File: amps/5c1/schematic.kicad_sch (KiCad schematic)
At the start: 21 parts, among them T1 SE 5k:8

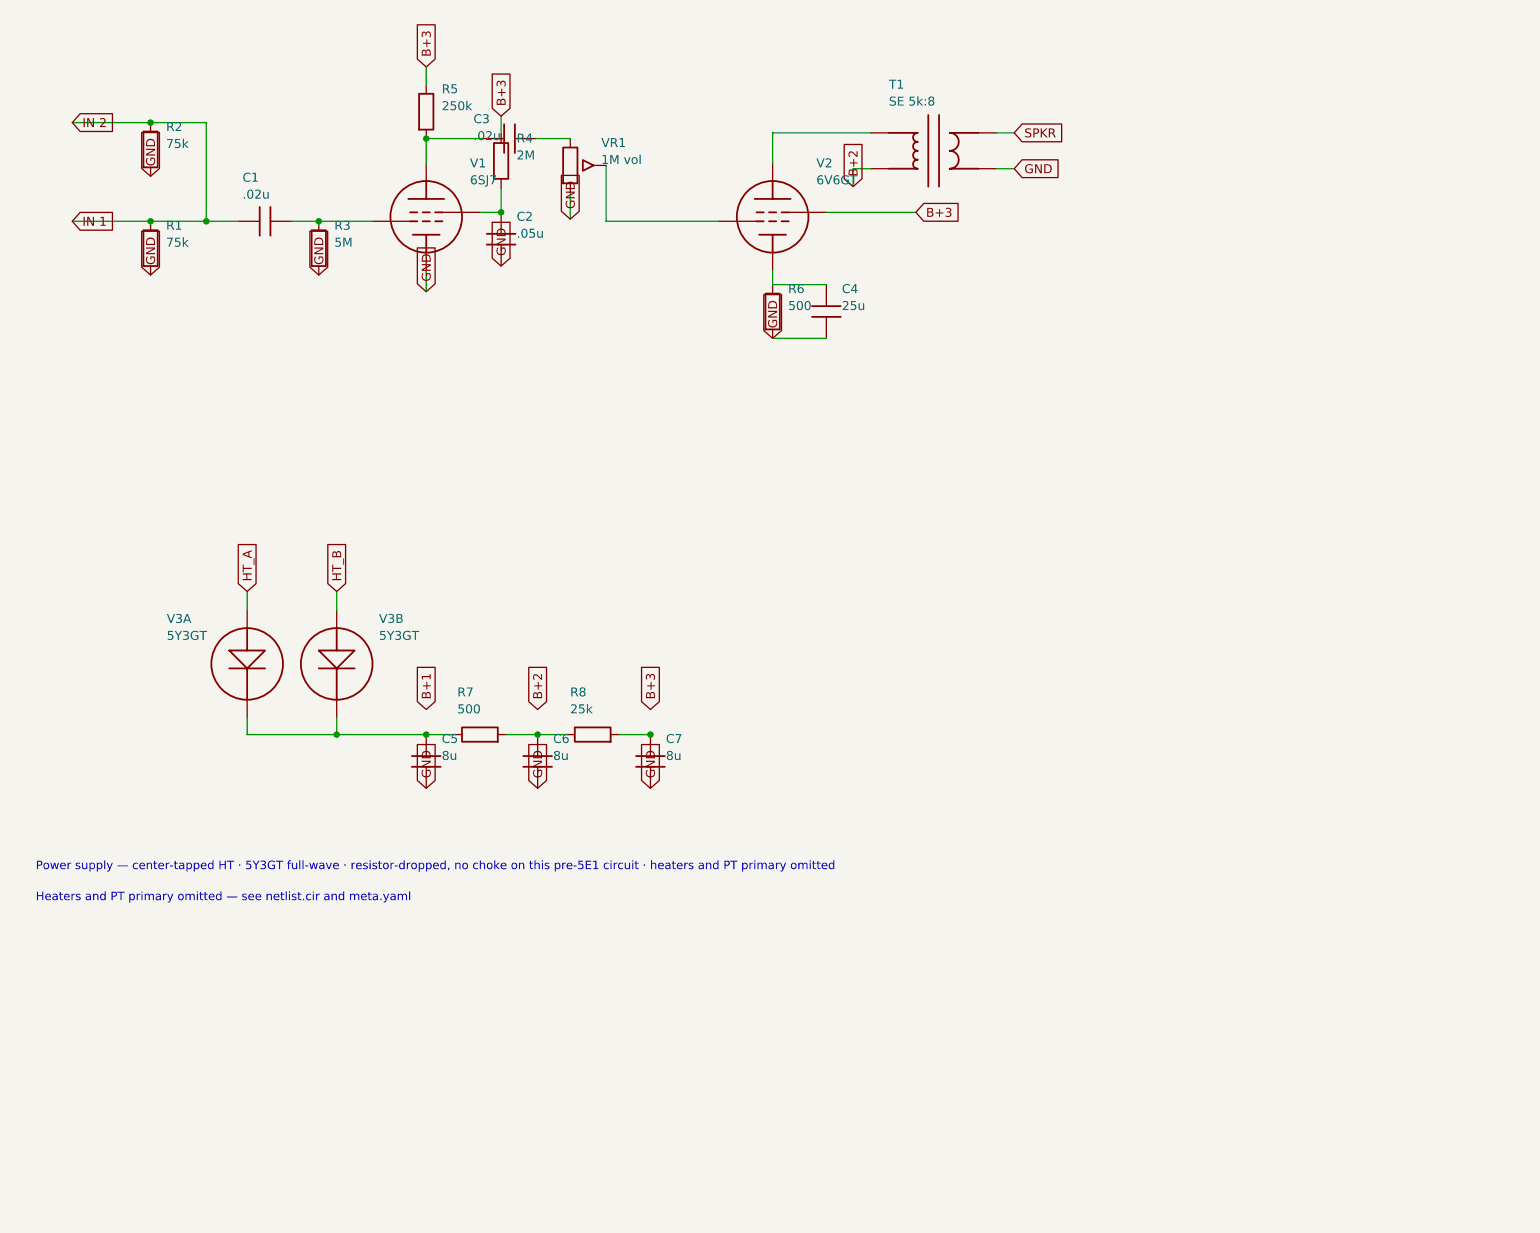
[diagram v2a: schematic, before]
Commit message: Fix: rotated global labels lettered their net names outside the flag
Every global label this pipeline emitted carried (justify left) regardless of
rotation. KiCanvas — like KiCad — draws label text horizontally at 0/180 and
vertically at 90/270 and reads WHICH SIDE of the anchor it letters on from the
justification, so at 180 and 270 the name printed outside an empty flag
outline, struck through by the very wire it names: 219 labels at 180 deg
(including the input-jack flags at top-left of nearly every sheet, the first
glyphs a visitor reads) and 792 GND/rail flags at 270 whose names squeezed at
the flag mouth instead of lettering down the body. The library already
compensated rotation for property text (`pa`); this mirrors that logic for
global labels: justify right at 180/270, left at 0/90.

check_schematics gains the geometry clause whose absence let all 1011
instances through a "no lettering through circuitry" pass: it modelled the
flag box but never the label TEXT, so a name rendered on the wrong side was
invisible to it. The gate now proves justification compensates rotation on
every global label.

Two more things this exposed, fixed in the same engine pass:

- Placement now measures with the renderer's own Newstroke advance table
  (extracted from the vendored kicanvas.js) instead of a flat 0.68-em prose
  average that under-read part lettering by a quarter — the mechanism behind
  every "metered clean, printed through its neighbour" incident. The GATE
  deliberately keeps the coarse ruler: re-ruling it with renderer truth was
  tried and red-flagged 28 of 34 sheets over abutments three visual passes
  had already judged sub-visual (the two-rulers note in schematic_lib.py).
- place_captions' escape ladder runs further, because a banner caption
  measured truly is half again wider than the old estimate believed.

All 34 schematics regenerated; full gate suite green.

🤖 Generated with [Claude Code](https://claude.com/claude-code)

Co-Authored-By: Claude Fable 5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
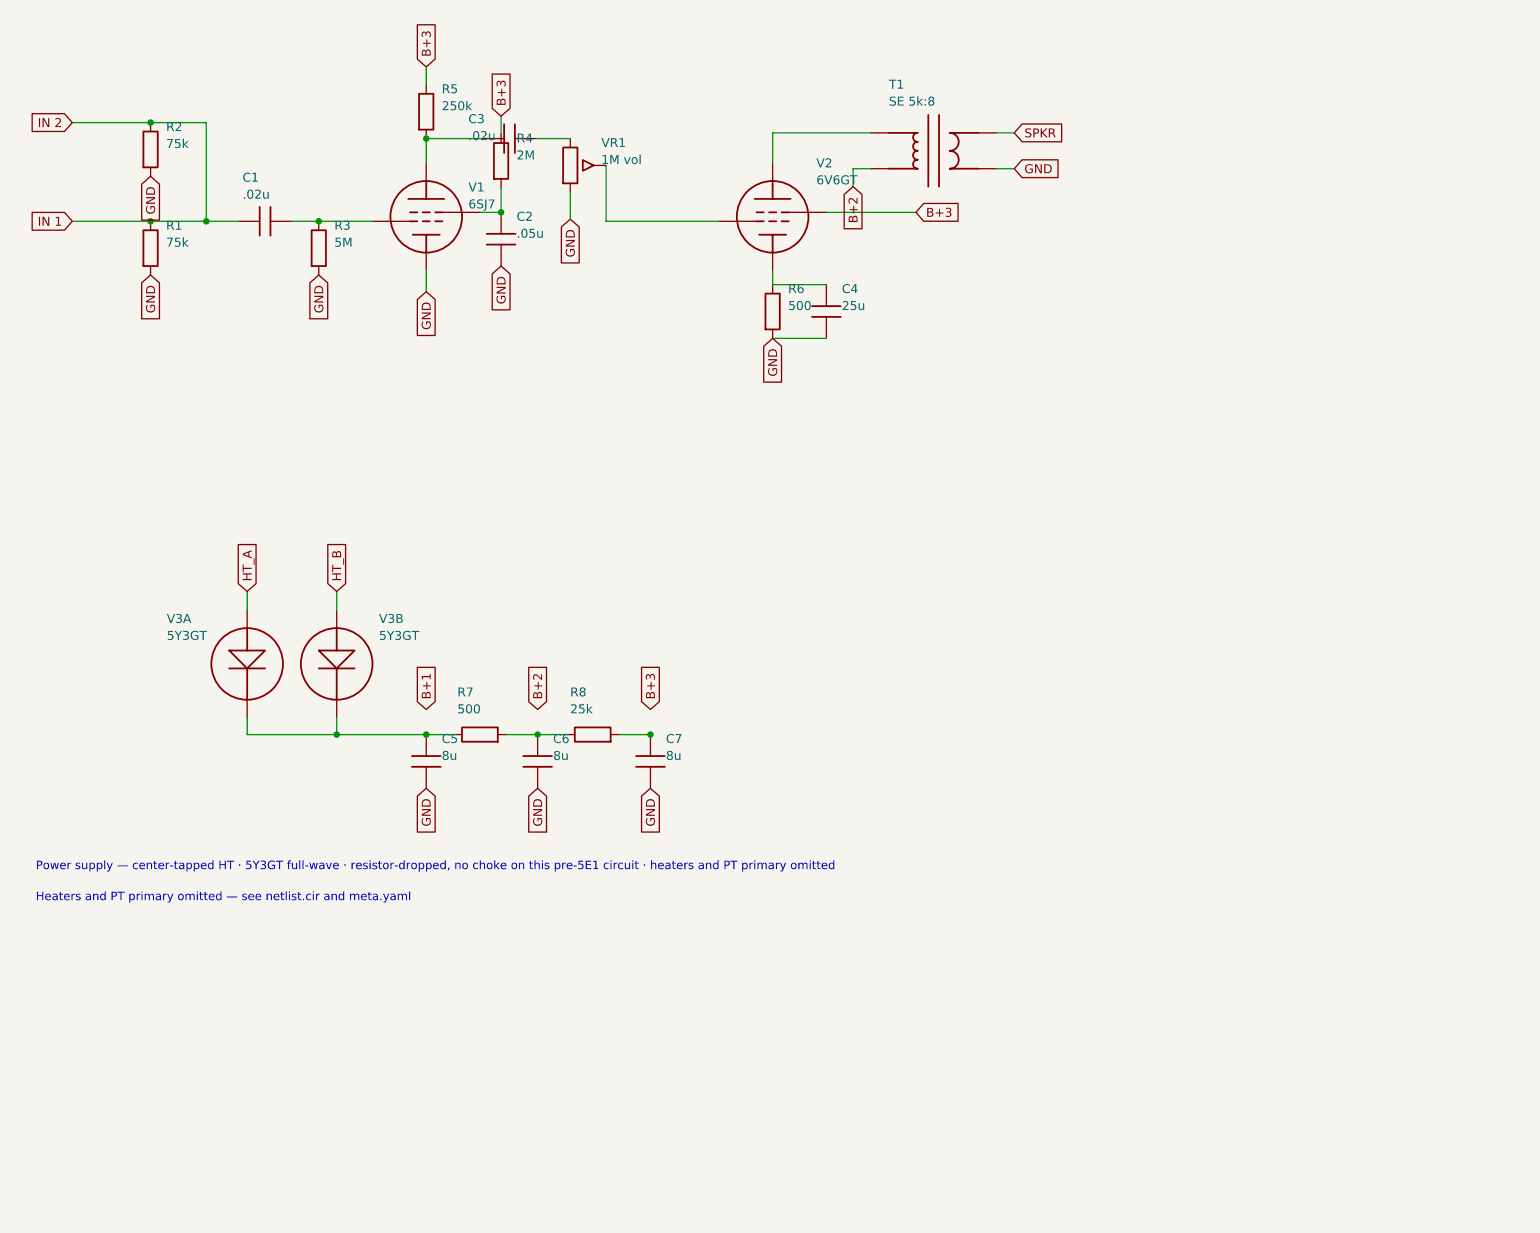
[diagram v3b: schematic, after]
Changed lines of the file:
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@@
     (comment 3 "Values read from: https://el34world.com/charts/Schematics/files/Fender/Fender_champ_5c1_schem.pdf"))
   (global_label "IN 1" (shape input) (at 17.8816 38.913 180)
-    (effects (font (size 1.27 1.27)) (justify left)))
+    (effects (font (size 1.27 1.27)) (justify right)))
   (wire (pts (xy 17.8816 38.913) (xy 28.9816 38.913))
     (stroke (width 0) (type default)))
@@
     (property "Value" "75k" (at 31.1816 41.923 0) (effects (font (size 1.27 1.27)) (justify left))))
   (global_label "GND" (shape input) (at 28.9816 46.533 270)
-    (effects (font (size 1.27 1.27)) (justify left)))
+    (effects (font (size 1.27 1.27)) (justify right)))
   (wire (pts (xy 28.9816 38.913) (xy 36.8816 38.913))
     (stroke (width 0) (type default)))
   (global_label "IN 2" (shape input) (at 17.8816 24.913 180)
-    (effects (font (size 1.27 1.27)) (justify left)))
+    (effects (font (size 1.27 1.27)) (justify right)))
   (wire (pts (xy 17.8816 24.913) (xy 28.9816 24.913))
     (stroke (width 0) (type default)))
@@
     (property "Value" "75k" (at 31.1816 27.923 0) (effects (font (size 1.27 1.27)) (justify left))))
   (global_label "GND" (shape input) (at 28.9816 32.533 270)
-    (effects (font (size 1.27 1.27)) (justify left)))
+    (effects (font (size 1.27 1.27)) (justify right)))
   (wire (pts (xy 28.9816 24.913) (xy 36.8816 24.913))
     (stroke (width 0) (type default)))
@@
     (property "Value" "5M" (at 55.0416 41.923 0) (effects (font (size 1.27 1.27)) (justify left))))
   (global_label "GND" (shape input) (at 52.8416 46.533 270)
-    (effects (font (size 1.27 1.27)) (justify left)))
+    (effects (font (size 1.27 1.27)) (justify right)))
   (wire (pts (xy 52.8416 38.913) (xy 60.4616 38.913))
     (stroke (width 0) (type default)))
   (symbol (lib_id "cx:PENTODE") (at 68.0816 38.278 0) (unit 1)
     (in_bom yes) (on_board yes)
-    (property "Reference" "V1" (at 74.2816 30.678 0) (effects (font (size 1.27 1.27)) (justify left)))
-    (property "Value" "6SJ7" (at 74.2816 33.078 0) (effects (font (size 1.27 1.27)) (justify left))))
+    (property "Reference" "V1" (at 74.0616 34.098 0) (effects (font (size 1.27 1.27)) (justify left)))
+    (property "Value" "6SJ7" (at 74.0616 36.498 0) (effects (font (size 1.27 1.27)) (justify left))))
   (wire (pts (xy 68.0816 45.898) (xy 68.0816 48.898))
     (stroke (width 0) (type default)))
   (global_label "GND" (shape input) (at 68.0816 48.898 270)
-    (effects (font (size 1.27 1.27)) (justify left)))
+    (effects (font (size 1.27 1.27)) (justify right)))
   (wire (pts (xy 68.0816 30.658) (xy 68.0816 27.178))
     (stroke (width 0) (type default)))
@@
   (symbol (lib_id "cx:C") (at 79.8916 27.178 90) (unit 1)
     (in_bom yes) (on_board yes)
-    (property "Reference" "C3" (at 74.7752 24.41 270) (effects (font (size 1.27 1.27)) (justify left)))
-    (property "Value" ".02u" (at 74.7752 26.81 270) (effects (font (size 1.27 1.27)) (justify left))))
+    (property "Reference" "C3" (at 74.0576 24.41 270) (effects (font (size 1.27 1.27)) (justify left)))
+    (property "Value" ".02u" (at 74.0576 26.81 270) (effects (font (size 1.27 1.27)) (justify left))))
   (wire (pts (xy 75.7016 37.643) (xy 78.7016 37.643))
     (stroke (width 0) (type default)))
@@
     (property "Value" ".05u" (at 80.9016 40.653 0) (effects (font (size 1.27 1.27)) (justify left))))
   (global_label "GND" (shape input) (at 78.7016 45.263 270)
-    (effects (font (size 1.27 1.27)) (justify left)))
+    (effects (font (size 1.27 1.27)) (justify right)))
   (wire (pts (xy 78.7016 37.643) (xy 78.7016 34.163))
     (stroke (width 0) (type default)))
@@
     (stroke (width 0) (type default)))
   (global_label "GND" (shape input) (at 88.5116 38.608 270)
-    (effects (font (size 1.27 1.27)) (justify left)))
+    (effects (font (size 1.27 1.27)) (justify right)))
   (wire (pts (xy 93.5916 30.988) (xy 93.5916 38.913))
     (stroke (width 0) (type default)))
@@
     (stroke (width 0) (type default)))
   (global_label "GND" (shape input) (at 117.212 55.518 270)
-    (effects (font (size 1.27 1.27)) (justify left)))
+    (effects (font (size 1.27 1.27)) (justify right)))
   (symbol (lib_id "cx:OT_SE") (at 140.052 28.913 0) (unit 1)
     (in_bom yes) (on_board yes)
@@
     (stroke (width 0) (type default)))
   (global_label "B+2" (shape input) (at 128.622 33.993 270)
-    (effects (font (size 1.27 1.27)) (justify left)))
+    (effects (font (size 1.27 1.27)) (justify right)))
   (wire (pts (xy 148.942 26.373) (xy 151.482 26.373))
     (stroke (width 0) (type default)))
@@
     (property "Value" "8u" (at 70.2816 114.723 0) (effects (font (size 1.27 1.27)) (justify left))))
   (global_label "GND" (shape input) (at 68.0816 119.333 270)
-    (effects (font (size 1.27 1.27)) (justify left)))
+    (effects (font (size 1.27 1.27)) (justify right)))
   (global_label "B+1" (shape input) (at 68.0816 108.153 90)
     (effects (font (size 1.27 1.27)) (justify left)))
@@
     (property "Value" "8u" (at 86.0816 114.723 0) (effects (font (size 1.27 1.27)) (justify left))))
   (global_label "GND" (shape input) (at 83.8816 119.333 270)
-    (effects (font (size 1.27 1.27)) (justify left)))
+    (effects (font (size 1.27 1.27)) (justify right)))
   (global_label "B+2" (shape input) (at 83.8816 108.153 90)
     (effects (font (size 1.27 1.27)) (justify left)))
@@
     (property "Value" "8u" (at 102.082 114.723 0) (effects (font (size 1.27 1.27)) (justify left))))
   (global_label "GND" (shape input) (at 99.8816 119.333 270)
-    (effects (font (size 1.27 1.27)) (justify left)))
+    (effects (font (size 1.27 1.27)) (justify right)))
   (global_label "B+3" (shape input) (at 99.8816 108.153 90)
     (effects (font (size 1.27 1.27)) (justify left)))

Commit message: Fix: deterministic schematic ids and wires split at every join
- _u() is uuid5 over (amp id, emission order), so a regeneration of an
  unchanged script is byte-identical and a drift gate becomes possible
- write() splits wire segments at symbol pins, wire ends and junction dots,
  so the file connects exactly what the drawing shows under KiCad's
  endpoint-only semantics (270 pins were on a wire's interior; net
  partitions unchanged on all 38 sheets)
- all sheets regenerated; aa864-bassman title block was stale (draft) and
  now matches meta.yaml (verified)

Co-Authored-By: Claude Fable 5.1 <noreply@anthropic.com>
Claude-Session: https://claude.ai/code/session_01KBMfdh37HmCL2iWcBiL5J1
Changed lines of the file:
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@@
   (wire (pts (xy 55.3816 109.313) (xy 55.3816 111.713))
     (stroke (width 0) (type default)))
-  (wire (pts (xy 42.6816 111.713) (xy 68.0816 111.713))
+  (wire (pts (xy 42.6816 111.713) (xy 55.3816 111.713))
+    (stroke (width 0) (type default)))
+  (wire (pts (xy 55.3816 111.713) (xy 68.0816 111.713))
     (stroke (width 0) (type default)))
   (junction (at 55.3816 111.713) (diameter 0) (color 0 0 0 0))

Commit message: Fix: schematic wiring on 5c1, 5e1, 5e4a, 5e5a, 5e6a, 5f4; all six claim equivalence
- 5c1, 5e1: the B+1/B+2/B+3 labels sat 3.56 mm above the filter chain with
  no lead, naming rails the drawing never reached
- 5e4a, 5e5a, 5e6a, 5f4: the 220k grid leak tapped the coupling-cap node;
  the netlist and the factory-derived layouts both return it at the grid
  pin after the 1.5k stopper (coupler -> stopper -> grid, as jtm45 draws
  it); each stopper now lands on the pentode's own grid pin and the leak
  hangs off that junction
- sch_map.yaml schematic_claim: verified on all six -> 37 of 38 sheets are
  hard-gated; 6g5 stays unclaimed (presence-branch DC path is a source
  question, not a declaration)

Co-Authored-By: Claude Fable 5.1 <noreply@anthropic.com>
Claude-Session: https://claude.ai/code/session_01KBMfdh37HmCL2iWcBiL5J1
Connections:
- net B+1: now also C5.1, R7.1, V3A.2 (K), V3B.2 (K)
- net B+2: now also C6.1, R7.2, R8.1
- net B+3: now also C7.1, R8.2
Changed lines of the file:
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@@
   (global_label "GND" (shape input) (at 68.0816 119.333 270)
     (effects (font (size 1.27 1.27)) (justify right)))
+  (wire (pts (xy 68.0816 108.153) (xy 68.0816 111.713))
+    (stroke (width 0) (type default)))
   (global_label "B+1" (shape input) (at 68.0816 108.153 90)
     (effects (font (size 1.27 1.27)) (justify left)))
@@
   (global_label "GND" (shape input) (at 83.8816 119.333 270)
     (effects (font (size 1.27 1.27)) (justify right)))
+  (wire (pts (xy 83.8816 108.153) (xy 83.8816 111.713))
+    (stroke (width 0) (type default)))
   (global_label "B+2" (shape input) (at 83.8816 108.153 90)
     (effects (font (size 1.27 1.27)) (justify left)))
@@
   (global_label "GND" (shape input) (at 99.8816 119.333 270)
     (effects (font (size 1.27 1.27)) (justify right)))
+  (wire (pts (xy 99.8816 108.153) (xy 99.8816 111.713))
+    (stroke (width 0) (type default)))
   (global_label "B+3" (shape input) (at 99.8816 108.153 90)
     (effects (font (size 1.27 1.27)) (justify left)))
